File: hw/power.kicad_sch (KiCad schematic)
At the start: 30 parts, among them J1 XT30PW-M bus IN, J2 XT30PW-F bus OUT, U1 LM5008A, U2 AP2112K-3.3

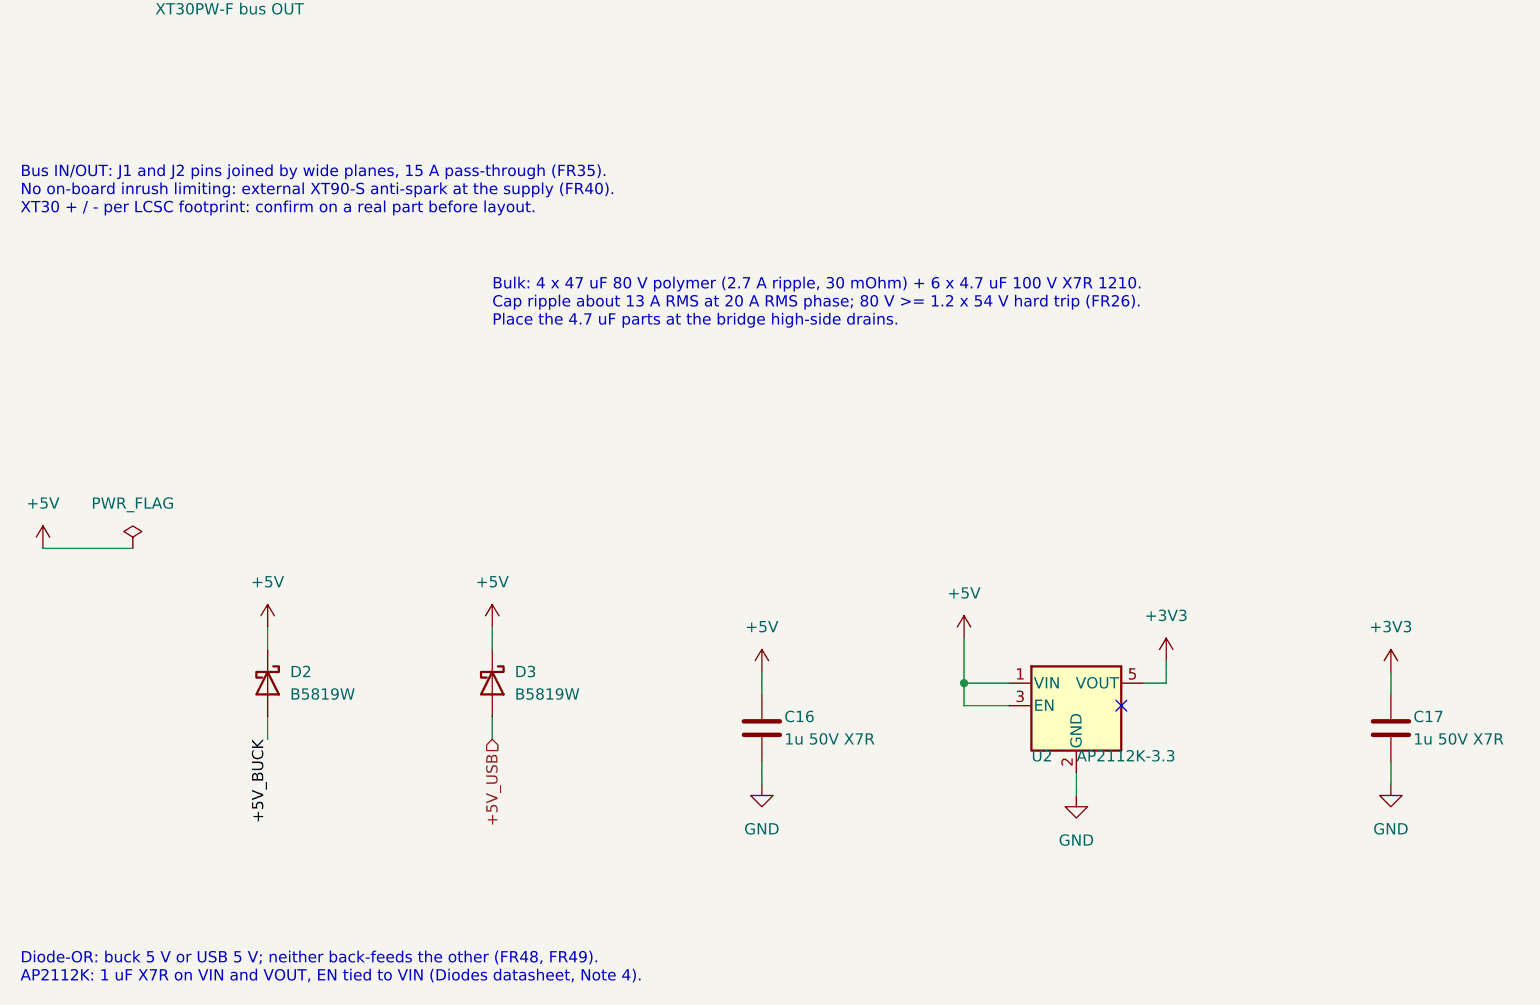
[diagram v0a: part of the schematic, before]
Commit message: Remove requirement IDs from schematic notes
Notes now state the reason in plain words so the schematic reads
without the requirements document.

Co-Authored-By: Claude Opus 5.5 <noreply@anthropic.com>
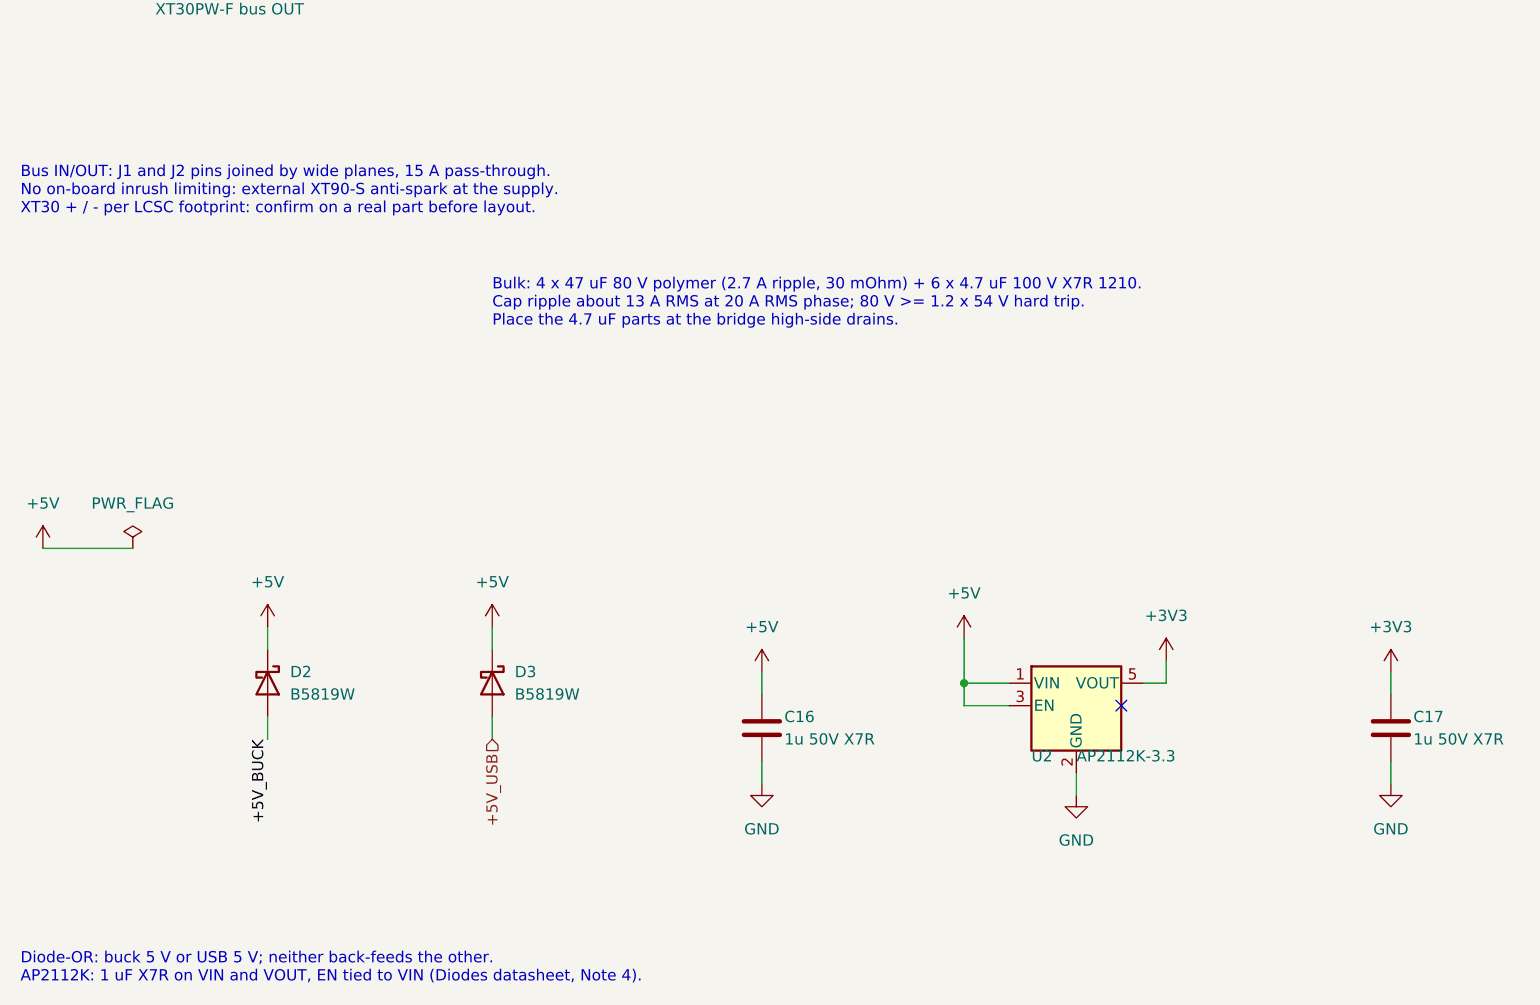
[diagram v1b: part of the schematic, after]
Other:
- note added: "Bulk: 4 x 47 uF 80 V polymer (2.7 A ripple, 30 mOhm) + 6 x 4.7 uF 100 V X7R 1210. Cap ripple about 13 A RMS at 20 A RMS phase; 80 V >= 1.2 x 54 V hard trip. Place the 4.7 uF parts at the bridge high-side drains."
- note added: "Bus IN/OUT: J1 and J2 pins joined by wide planes, 15 A pass-through. No on-board inrush limiting: external XT90-S anti-spark at the supply. XT30 + / - per LCSC footprint: confirm on a real part before layout."
- note added: "Diode-OR: buck 5 V or USB 5 V; neither back-feeds the other. AP2112K: 1 uF X7R on VIN and VOUT, EN tied to VIN (Diodes datasheet, Note 4)."
- note removed: "Bulk: 4 x 47 uF 80 V polymer (2.7 A ripple, 30 mOhm) + 6 x 4.7 uF 100 V X7R 1210. Cap ripple about 13 A RMS at 20 A RMS phase; 80 V >= 1.2 x 54 V hard trip (FR26). Place the 4.7 uF parts at the bridge high-side drains."
- note removed: "Bus IN/OUT: J1 and J2 pins joined by wide planes, 15 A pass-through (FR35). No on-board inrush limiting: external XT90-S anti-spark at the supply (FR40). XT30 + / - per LCSC footprint: confirm on a real part before layout."
- note removed: "Diode-OR: buck 5 V or USB 5 V; neither back-feeds the other (FR48, FR49). AP2112K: 1 uF X7R on VIN and VOUT, EN tied to VIN (Diodes datasheet, Note 4)."
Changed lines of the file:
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@@
 		(at 147.32 213.36)
 	)
-	(text "Bus IN/OUT: J1 and J2 pins joined by wide planes, 15 A pass-through (FR35).\nNo on-board inrush limiting: external XT90-S anti-spark at the supply (FR40).\nXT30 + / - per LCSC footprint: confirm on a real part before layout."
+	(text "Bus IN/OUT: J1 and J2 pins joined by wide planes, 15 A pass-through.\nNo on-board inrush limiting: external XT90-S anti-spark at the supply.\nXT30 + / - per LCSC footprint: confirm on a real part before layout."
 		(exclude_from_sim no)
 		(at 22.86 152.4 0.0000)
@@
 		)
 	)
-	(text "Bulk: 4 x 47 uF 80 V polymer (2.7 A ripple, 30 mOhm) + 6 x 4.7 uF 100 V X7R 1210.\nCap ripple about 13 A RMS at 20 A RMS phase; 80 V >= 1.2 x 54 V hard trip (FR26).\nPlace the 4.7 uF parts at the bridge high-side drains."
+	(text "Bulk: 4 x 47 uF 80 V polymer (2.7 A ripple, 30 mOhm) + 6 x 4.7 uF 100 V X7R 1210.\nCap ripple about 13 A RMS at 20 A RMS phase; 80 V >= 1.2 x 54 V hard trip.\nPlace the 4.7 uF parts at the bridge high-side drains."
 		(exclude_from_sim no)
 		(at 76.2 165.1 0.0000)
@@
 		)
 	)
-	(text "Diode-OR: buck 5 V or USB 5 V; neither back-feeds the other (FR48, FR49).\nAP2112K: 1 uF X7R on VIN and VOUT, EN tied to VIN (Diodes datasheet, Note 4)."
+	(text "Diode-OR: buck 5 V or USB 5 V; neither back-feeds the other.\nAP2112K: 1 uF X7R on VIN and VOUT, EN tied to VIN (Diodes datasheet, Note 4)."
 		(exclude_from_sim no)
 		(at 22.86 241.3 0.0000)

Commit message: Apply schematic review fixes and connector changes
- Remove the RC snubber pads (ringing handled by layout and IDRIVE)
  and renumber R/C references to close the gap.
- CAN connectors: JST-GH 3-pin (CANH, CANL, GND).
- Power connectors: XT30PW-F female for both bus IN and OUT so the
  live side of every link is shrouded; polarity checked on a real
  part (pad 1 GND under the rounded end, pad 2 VBUS under the flat
  end). Male XT30 footprint, model and datasheet removed.
- AS5047P CSn 10k pull-up so encoder inputs never float while the
  MCU is in reset or ROM DFU.
- LM5008A RT 180k -> 240k: on-time stays >= 400 ns at 54 V across
  the TON spread.
- Every BOM line checked in stock against JLCPCB's assembly library.
- Kelvin-tap placement added to the layout rules.

Co-Authored-By: Claude Opus 5.5 <noreply@anthropic.com>
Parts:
- removed J1: XT30PW-M bus IN, foc_controller:CONN-TH_XT30PW-M, symbol foc_controller:XT30PW-M
- added J1: XT30PW-F bus IN, foc_controller:CONN-TH_XT30PW-F-1, symbol foc_controller:XT30PW-F
- R1: value 180k 1% -> 240k 1%; LCSC C22827 -> C137765; MPN 0603WAF1803T5E -> RC0603FR-07240KL
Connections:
- net GND: now also J1.1 (-)
- net VBUS: now also J1.2 (+)
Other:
- note added: "Bus IN/OUT: J1 and J2 pins joined by wide planes, 15 A pass-through. No on-board inrush limiting: external XT90-S anti-spark at the supply. Both female (shrouded live side); chain leads are male-male. Pad 2 = + (flat end), pad 1 = - (rounded end)."
- note added: "LM5008A buck, 5 V out, 10 to 52 V in (SNVS583H 8.2 procedure, Fig. 10 topology): VOUT = 2.5 V x (R4 + R3) / R4 = 5.0 V (R3 = RFB2 VOUT-FB, R4 = RFB1 FB-GND) R1 = RT 240k: Fs = VOUT / (1.385e-10 x RT) = 150 kHz; ton at 54 V = 616 ns, 410 ns at the -33% TON spread > 400 ns L1 = 120 uH: ripple 250 mA p-p at 54 V; Isat 850 mA > 610 mA max current limit R2 = RCL 383k: Toff = 1e-5 / (0.285 + 2.5 / (6.3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"
- note removed: "Bus IN/OUT: J1 and J2 pins joined by wide planes, 15 A pass-through. No on-board inrush limiting: external XT90-S anti-spark at the supply. XT30 + / - per LCSC footprint: confirm on a real part before layout."
- note removed: "LM5008A buck, 5 V out, 10 to 52 V in (SNVS583H 8.2 procedure, Fig. 10 topology): VOUT = 2.5 V x (R4 + R3) / R4 = 5.0 V (R3 = RFB2 VOUT-FB, R4 = RFB1 FB-GND) R1 = RT 180k: Fs = VOUT / (1.385e-10 x RT) = 200 kHz; ton at 52 V = 479 ns > 400 ns L1 = 120 uH: ripple 188 mA p-p at 52 V; Isat 850 mA > 610 mA max current limit R2 = RCL 383k: Toff = 1e-5 / (0.285 + 2.5 / (6.35e-6 x RCL)) = 7.5 us R5 = 1 Oh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"

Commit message: Place the 45 x 45 mm two-sided board and review its risks
Ceramic-only bulk caps, per-phase caps under each FET pair, one FET row,
corner M3 holes, USB-C and CAN on the motor side, XT30s closer together.
Encoder clearance 10 mm, 10 A RMS rating with no heatsink. Placement
fixes from the risk review: BOOT0 pad away from VBUS, 3 mm clear around
the XT30 power joints, edge caps parallel to the edge. Specs, layout
check and risk review updated; fuse and regen clamp now required
off-board parts.

Co-Authored-By: Claude Opus 5.5 <noreply@anthropic.com>
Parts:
- added C44, C45, C46, C47, C48, C49: 4.7u 100V X7R, Capacitor_SMD:C_1210_3225Metric, symbol Device:C
- added C50, C51, C52: 100n 100V X7R, Capacitor_SMD:C_0603_1608Metric, symbol Device:C
- C1, C2, C3, C4: value 47u 80V polymer -> 4.7u 100V X7R; footprint foc_controller:CAP-SMD_BD10.0-L10.3-W10.3-FD -> Capacitor_SMD:C_1210_3225Metric; symbol Device:C_Polarized -> Device:C; LCSC C54321633 -> C381466; MPN MA80V47M10X10 -> FS32X475K101EGG
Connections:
- net GND: now also C44.2, C45.2, C46.2, C47.2, C48.2, C49.2, C50.2, C51.2, C52.2
- net VBUS: now also C44.1, C45.1, C46.1, C47.1, C48.1, C49.1, C50.1, C51.1, C52.1
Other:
- note added: "Bulk: 16 x 4.7 uF 100 V X7R 1210 (C1-C10, C44-C49), about 2 uF each at 48 V. No electrolytic: the ceramics carry the ~13 A RMS ripple at 20 A RMS phase (about 0.8 A each). 100 V >= 1.5 x 54 V. C1 / C5 / C9 and C50 / C51 / C52 (100 nF 0603) sit at each half-bridge (HS drain to shunt GND end); the rest are bulk beside the FET row. Chain-cable damping is verified on the bench."
- note removed: "Bulk: 4 x 47 uF 80 V polymer (2.7 A ripple, 30 mOhm) + 6 x 4.7 uF 100 V X7R 1210. Cap ripple about 13 A RMS at 20 A RMS phase; 80 V >= 1.2 x 54 V hard trip. Place the 4.7 uF parts at the bridge high-side drains."

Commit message: Route the 6-layer board and finalize parts for ordering
The 45 x 45 mm board is fully routed on six layers (F / GND / SIG /
SIG / PWR / B, 2 oz outer, 1 oz inner): DRC 0 errors, 0 unconnected,
schematic parity 0. Four layers could not route the DRV-to-MCU links
without moving the power or input stage.

- Encoder shares the DRV8353's SPI3 bus, as on the PoC; PA5-PA7 are
  unused. R25 pulls DRV nSCS up, since the DRV's logic inputs have an
  internal pull-down. The SDO / MISO pin-type warning is an ERC
  exclusion with a note.
- MCU is now the STM32G473CEU6: the G474 without the unused HRTIM,
  checked pin for pin against both datasheets, in stock and cheaper.
- Male XT30PW-M power connectors, HCS1206 shunts, SWD pads at the
  board edge.
- Design doc and review notes updated for the new stack-up, shared
  bus and MCU.

Co-Authored-By: Claude Opus 5.5 <noreply@anthropic.com>
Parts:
- J1: value XT30PW-F bus IN -> XT30PW-M bus IN; footprint foc_controller:CONN-TH_XT30PW-F-1 -> foc_controller:CONN-TH_XT30PW-M-1; symbol foc_controller:XT30PW-F -> foc_controller:XT30PW-M; LCSC C2913282 -> C431092; MPN XT30PW-F20.G.Y -> XT30PW-M30.G.Y
- J2: value XT30PW-F bus OUT -> XT30PW-M bus OUT; footprint foc_controller:CONN-TH_XT30PW-F-1 -> foc_controller:CONN-TH_XT30PW-M-1; symbol foc_controller:XT30PW-F -> foc_controller:XT30PW-M; LCSC C2913282 -> C431092; MPN XT30PW-F20.G.Y -> XT30PW-M30.G.Y
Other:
- note added: "Bus IN/OUT: J1 and J2 pins joined by wide planes, 15 A pass-through. No on-board inrush limiting: external XT90-S anti-spark at the supply. Both male (XT30PW-M); chain leads are female-female. Pad 2 = + (flat, chamfered end), pad 1 = - (rounded end)."
- note removed: "Bus IN/OUT: J1 and J2 pins joined by wide planes, 15 A pass-through. No on-board inrush limiting: external XT90-S anti-spark at the supply. Both female (shrouded live side); chain leads are male-male. Pad 2 = + (flat end), pad 1 = - (rounded end)."
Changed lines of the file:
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@@
 		)
 	)
-	(text "Bus IN/OUT: J1 and J2 pins joined by wide planes, 15 A pass-through.\nNo on-board inrush limiting: external XT90-S anti-spark at the supply.\nBoth female (shrouded live side); chain leads are male-male. Pad 2 = + (flat end), pad 1 = - (rounded end)."
+	(text "Bus IN/OUT: J1 and J2 pins joined by wide planes, 15 A pass-through.\nNo on-board inrush limiting: external XT90-S anti-spark at the supply.\nBoth male (XT30PW-M); chain leads are female-female. Pad 2 = + (flat, chamfered end), pad 1 = - (rounded end)."
 		(exclude_from_sim no)
 		(at 22.86 165.1 0)
@@
 	)
 	(symbol
-		(lib_id "foc_controller:XT30PW-F")
+		(lib_id "foc_controller:XT30PW-M")
 		(at 45.72 66.04 0)
 		(unit 1)
@@
 			)
 		)
-		(property "Value" "XT30PW-F bus IN"
+		(property "Value" "XT30PW-M bus IN"
 			(at 38.1 78.74 0)
 			(show_name no)
@@
 			)
 		)
-		(property "Footprint" "foc_controller:CONN-TH_XT30PW-F-1"
+		(property "Footprint" "foc_controller:CONN-TH_XT30PW-M-1"
 			(at 45.72 66.04 0)
 			(hide yes)
@@
 			)
 		)
-		(property "LCSC" "C2913282"
+		(property "LCSC" "C431092"
 			(at 48.26 71.1199 0)
 			(hide yes)
@@
 			)
 		)
-		(property "MPN" "XT30PW-F20.G.Y"
+		(property "MPN" "XT30PW-M30.G.Y"
 			(at 48.26 71.1199 0)
 			(hide yes)
@@
 	)
 	(symbol
-		(lib_id "foc_controller:XT30PW-F")
+		(lib_id "foc_controller:XT30PW-M")
 		(at 45.72 121.92 0)
 		(unit 1)
@@
 			)
 		)
-		(property "Value" "XT30PW-F bus OUT"
+		(property "Value" "XT30PW-M bus OUT"
 			(at 38.1 134.62 0)
 			(show_name no)
@@
 			)
 		)
-		(property "Footprint" "foc_controller:CONN-TH_XT30PW-F-1"
+		(property "Footprint" "foc_controller:CONN-TH_XT30PW-M-1"
 			(at 45.72 121.92 0)
 			(hide yes)
@@
 			)
 		)
-		(property "LCSC" "C2913282"
+		(property "LCSC" "C431092"
 			(at 48.26 126.9999 0)
 			(hide yes)
@@
 			)
 		)
-		(property "MPN" "XT30PW-F20.G.Y"
+		(property "MPN" "XT30PW-M30.G.Y"
 			(at 48.26 126.9999 0)
 			(hide yes)
